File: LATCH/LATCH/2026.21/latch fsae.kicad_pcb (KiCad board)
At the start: 2 copper layers, 105.8 x 80.8 mm, 40 parts, among them J1 39281123, J4 39281083, J5 39281063, K1 G6B-2214P-US DC12, K2 G6B-2214P-US DC12, K4 G6B-2214P-US DC12, Q1 PMOS IRF9540, Q2 PMOS IRF9540, Q3 PMOS IRF9540, SW1 SW_Push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

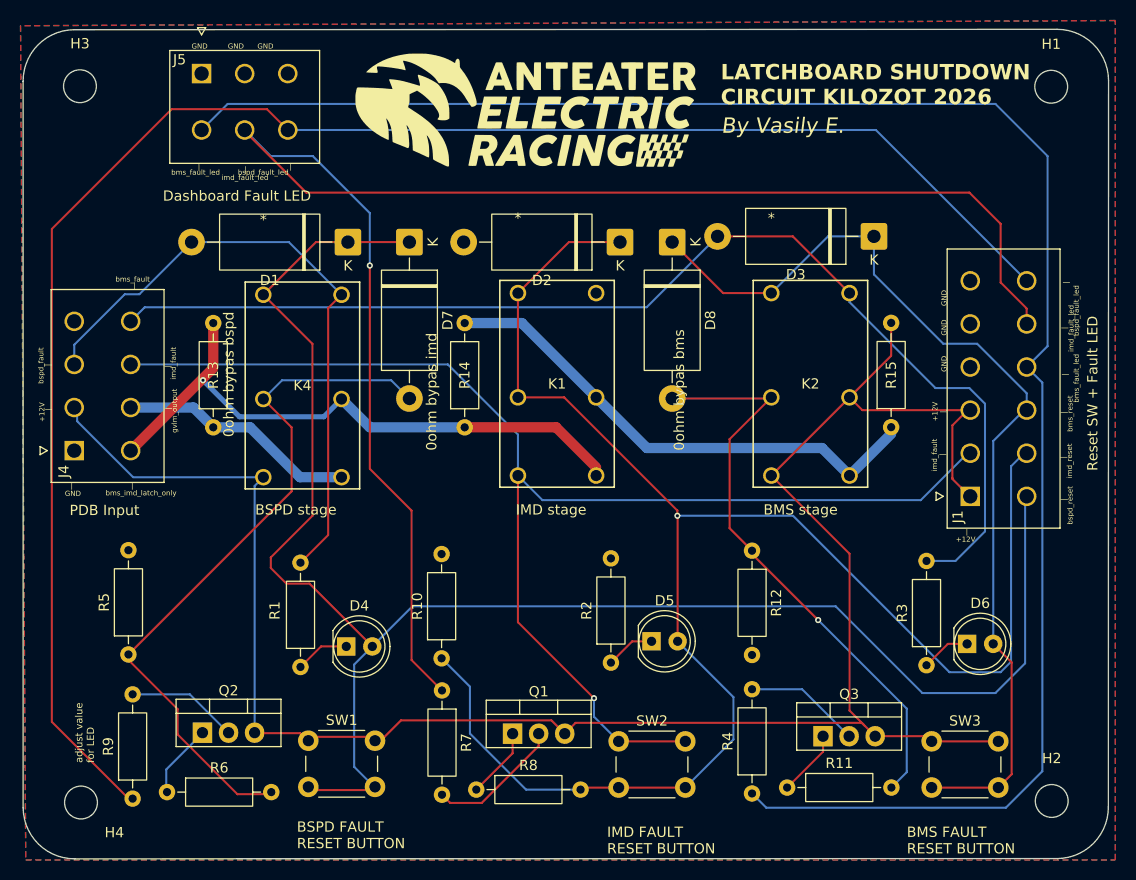
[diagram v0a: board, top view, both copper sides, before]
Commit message: swaped pins on relay
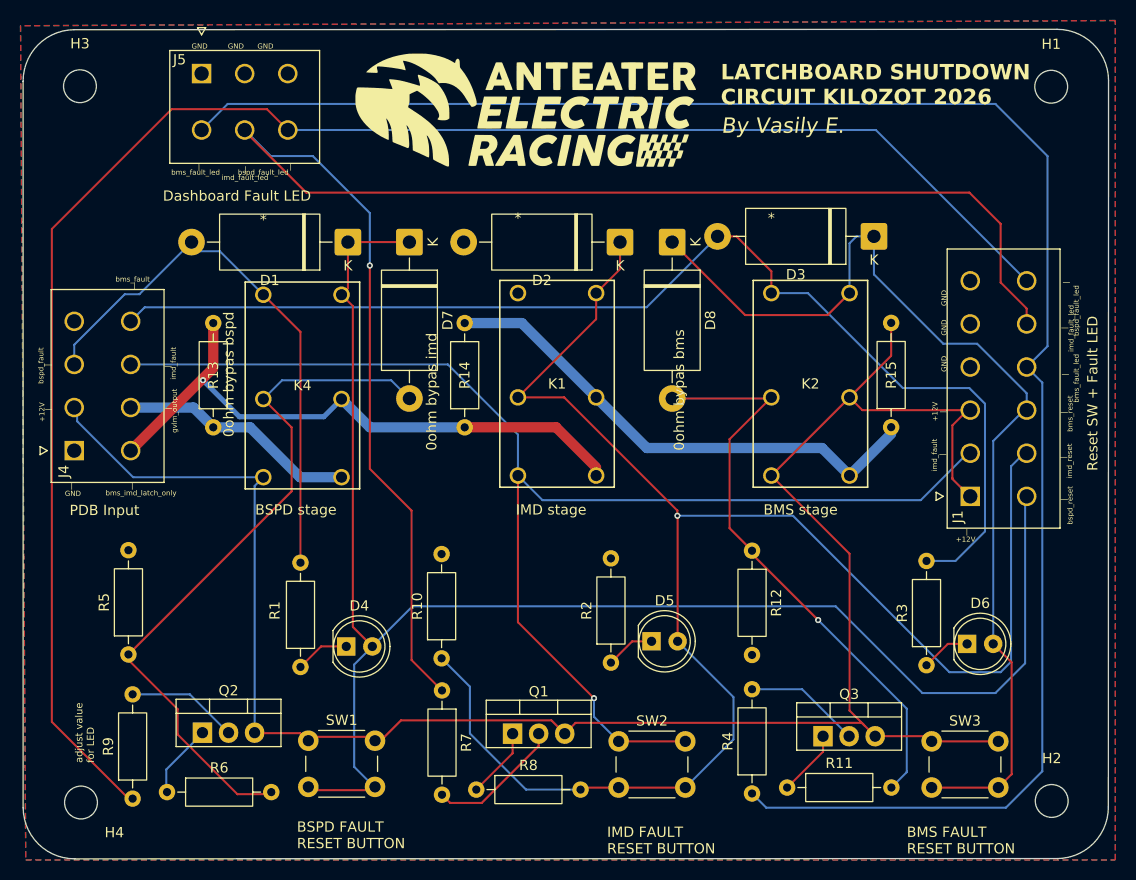
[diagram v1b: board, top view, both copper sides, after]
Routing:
- net bspd_reset: track 168.2 -> 154.6 mm
- net BSPD_FAULT: track 62.0 -> 54.2 mm
- net bms_reset: track 95.9 -> 100.3 mm
- net imd_reset: track 164.3 -> 162.2 mm
- net BMS_FAULT: track 113.3 -> 113.9 mm
